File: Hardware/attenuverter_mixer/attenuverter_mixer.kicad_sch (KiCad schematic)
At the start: 54 parts, among them J1 euro_power_10, J10 thonkiconn, J2 thonkiconn, J3 thonkiconn, J4 thonkiconn, J5 thonkiconn, J6 thonkiconn, J7 thonkiconn, J8 thonkiconn, J9 thonkiconn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

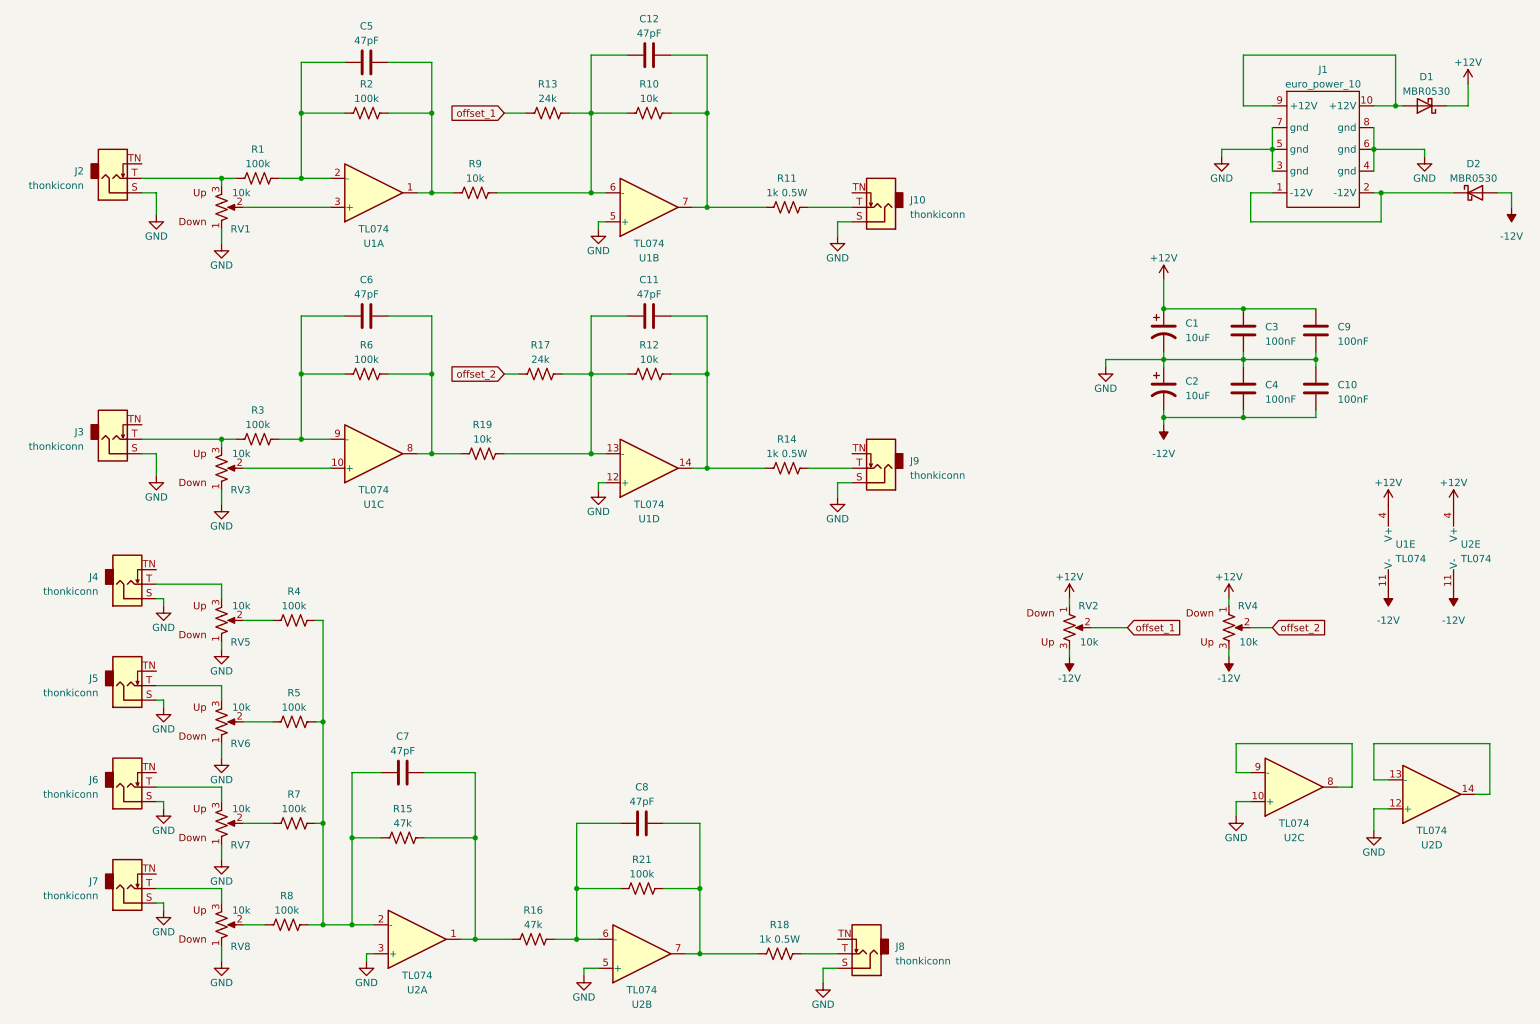
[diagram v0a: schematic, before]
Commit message: attenuverter complete
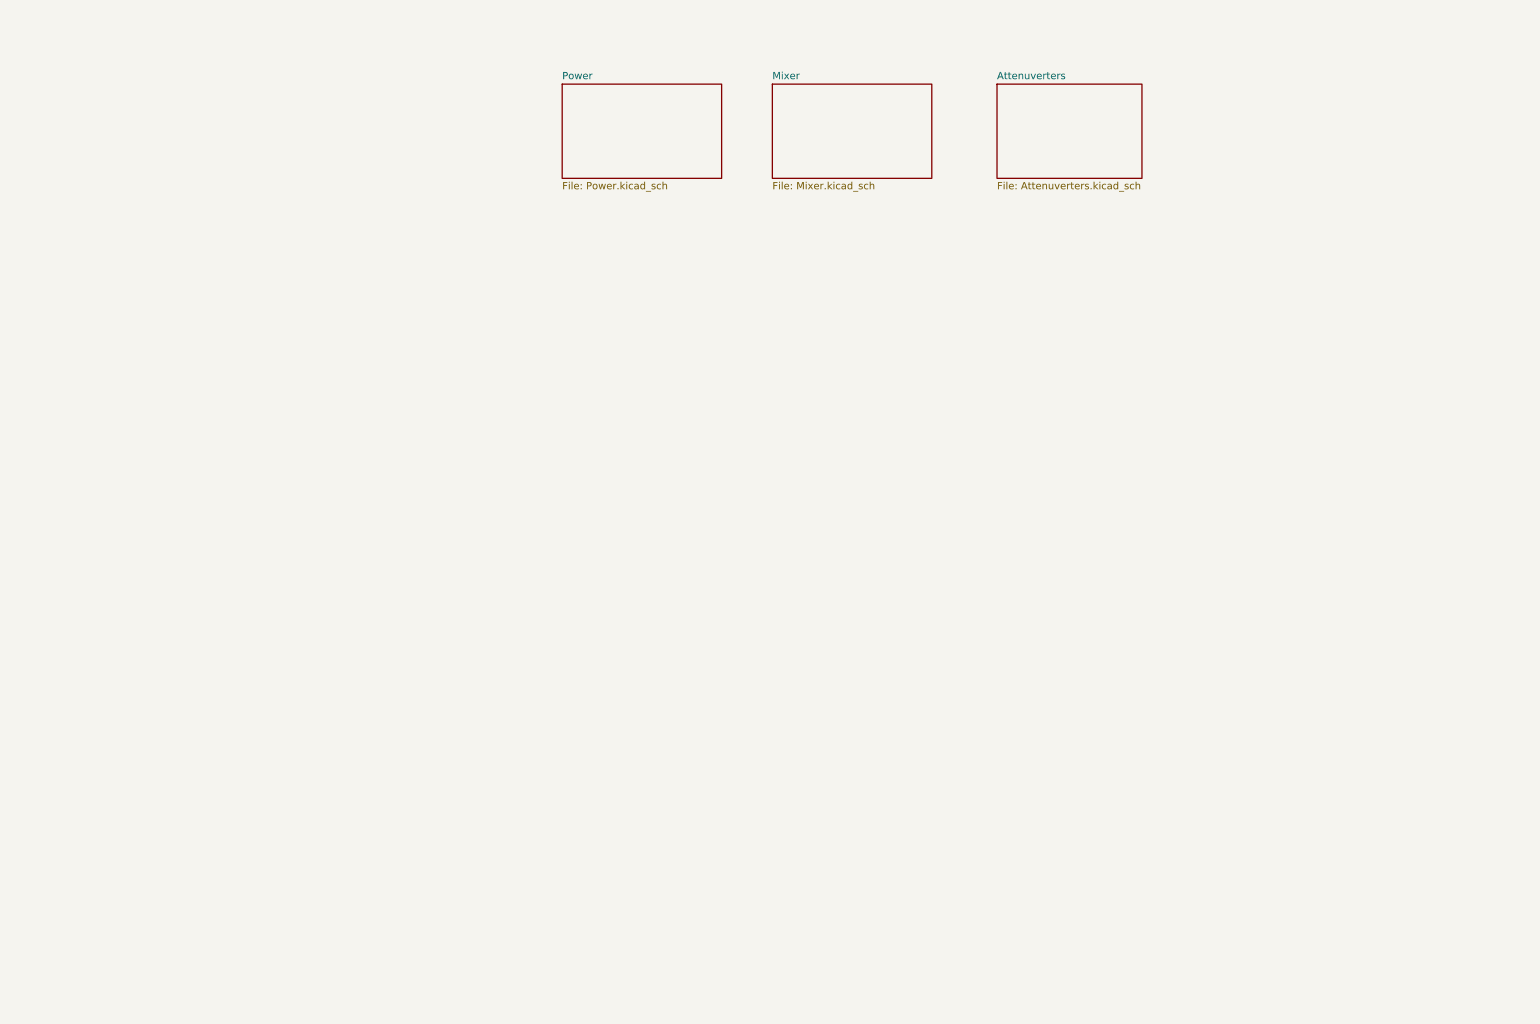
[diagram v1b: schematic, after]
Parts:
- removed C1, C2: 10uF, Capacitor_SMD:CP_Elec_5x5.3, symbol synthesis:CAP_10UF_POL_SMD
- removed C10, C3, C4, C9: 100nF, Capacitor_SMD:C_0201_0603Metric, symbol synthesis:CAP_100NF_0603_X7R
- removed C11, C12, C5, C6, C7, C8: 47pF, Capacitor_SMD:C_0201_0603Metric, symbol synthesis:CAP_47PF_0603_COG
- removed D1, D2: MBR0530, Diode_SMD:D_SOD-123, symbol Diode:MBR0530
- removed J1: euro_power_10, synthesis:eurorack_10, symbol synthesis:euro_power_10
- removed J10, J2, J3, J4, J5, J6, J7, J8, J9: thonkiconn, Connector_Audio:Jack_3.5mm_QingPu_WQP-PJ398SM_Vertical_CircularHoles, symbol synthesis:thonkiconn
- removed R1, R2, R21, R3, R4, R5, R6, R7, R8: 100k, Resistor_SMD:R_0603_1608Metric, symbol synthesis:RES_100k_0603
- removed R10, R12, R19, R9: 10k, Resistor_SMD:R_0603_1608Metric, symbol synthesis:RES_10K_0603
- removed R11, R14, R18: 1k 0.5W, Resistor_SMD:R_1210_3225Metric, symbol synthesis:RES_1K_1210
- removed R13, R17: 24k, Resistor_SMD:R_0603_1608Metric, symbol synthesis:RES_24K_0603
- removed R15, R16: 47k, Resistor_SMD:R_0603_1608Metric, symbol synthesis:RES_47K_0603
- removed RV1, RV2, RV3, RV4, RV5, RV6, RV7, RV8: 10k, Potentiometer_THT:Potentiometer_Alpha_RD901F-40-00D_Single_Vertical, symbol synthesis:ALPHAPOT_10K
- removed U1, U2: TL074, Package_SO:TSSOP-14_4.4x5mm_P0.65mm, symbol synthesis:TL074
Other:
- added sheet Attenuverters (Attenuverters.kicad_sch)
- added sheet Mixer (Mixer.kicad_sch)
- added sheet Power (Power.kicad_sch)
